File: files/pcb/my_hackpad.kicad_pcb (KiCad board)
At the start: 2 copper layers, 132 x 101.5 mm, 32 parts, among them SW1 CherryMX, SW10 CherryMX, SW11 CherryMX, SW12 CherryMX, SW13 CherryMX, SW14 CherryMX, SW15 CherryMX, SW16 RotaryEncoder_Switch, SW2 CherryMX, SW3 CherryMX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

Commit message: Actual gnd plane fixed
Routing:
- net GND: track 56.5 -> 0.00 mm
- added copper zone on B.Cu, net GND
- added copper zone on F.Cu, net GND
- removed copper zone on B.Cu, net (none)
- removed copper zone on F.Cu, net (none)
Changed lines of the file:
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@@
-	)
-	(segment
-		(start 131.306 59.17)
-		(end 133.806 61.67)
-		(width 0.25)
-		(layer "B.Cu")
-		(net 24)
-	)
-	(segment
-		(start 93.676015 50.66575)
-		(end 93.676015 57.100015)
-		(width 0.25)
-		(layer "B.Cu")
-		(net 24)
-	)
-	(segment
-		(start 98.032 59.182)
-		(end 98.044 59.17)
-		(width 0.25)
-		(layer "B.Cu")
-		(net 24)
-	)
-	(segment
-		(start 127.12 59.17)
-		(end 98.044 59.17)
-		(width 0.25)
-		(layer "B.Cu")
-		(net 24)
-	)
-	(segment
-		(start 95.758 59.182)
-		(end 98.032 59.182)
-		(width 0.25)
-		(layer "B.Cu")
-		(net 24)
-	)
-	(segment
-		(start 127.12 59.17)
-		(end 131.306 59.17)
-		(width 0.25)
-		(layer "B.Cu")
-		(net 24)
-	)
-	(segment
-		(start 133.806 61.67)
-		(end 141.62 61.67)
-		(width 0.25)
-		(layer "B.Cu")
-		(net 24)
-	)
-	(segment
-		(start 98.044 59.17)
-		(end 97.778 59.17)
-		(width 0.25)
-		(layer "B.Cu")
-		(net 24)
-	)
-	(segment
-		(start 93.676015 57.100015)
-		(end 95.758 59.182)
-		(width 0.25)
-		(layer "B.Cu")
-		(net 24)
 	)
 	(segment
@@
 	)
 	(zone
-		(net 0)
-		(net_name "")
+		(net 24)
+		(net_name "GND")
 		(layers "F&B.Cu")
 		(name "GND Plane")

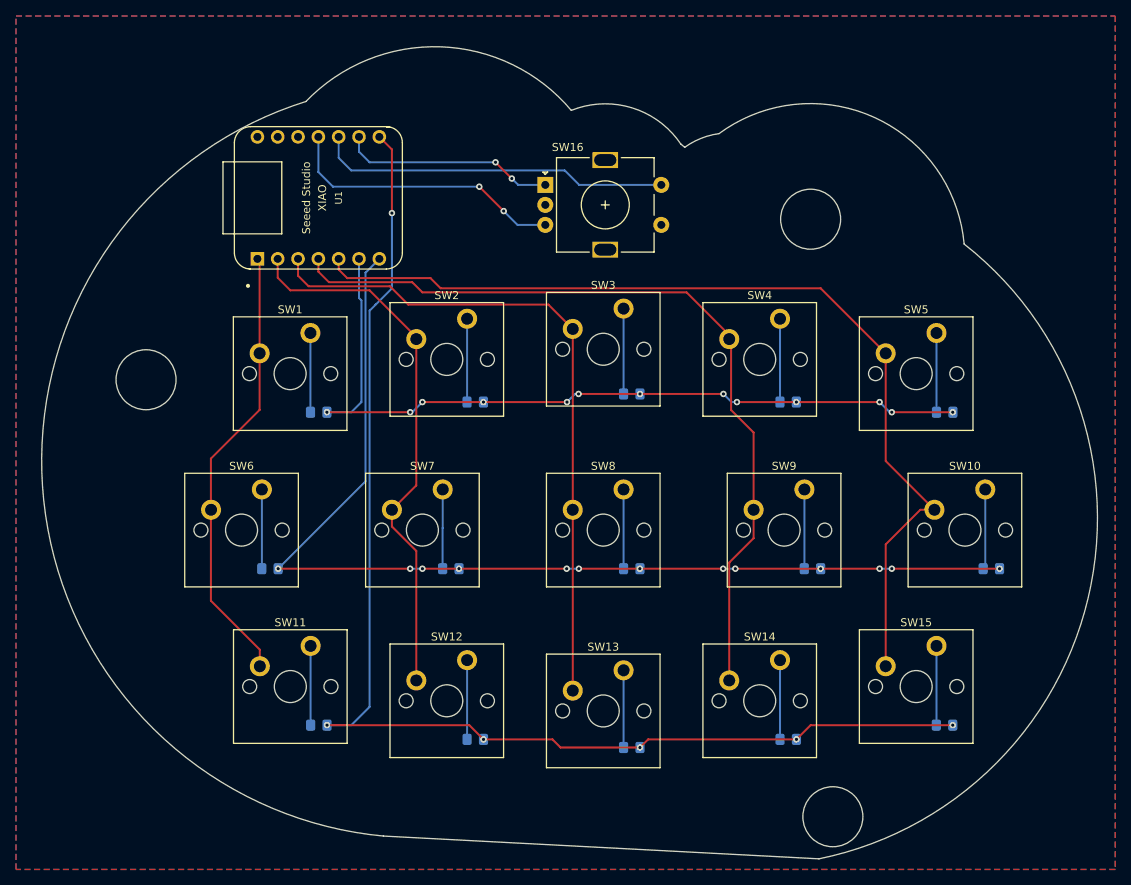
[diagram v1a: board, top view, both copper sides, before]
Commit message: PCB wire traces updated
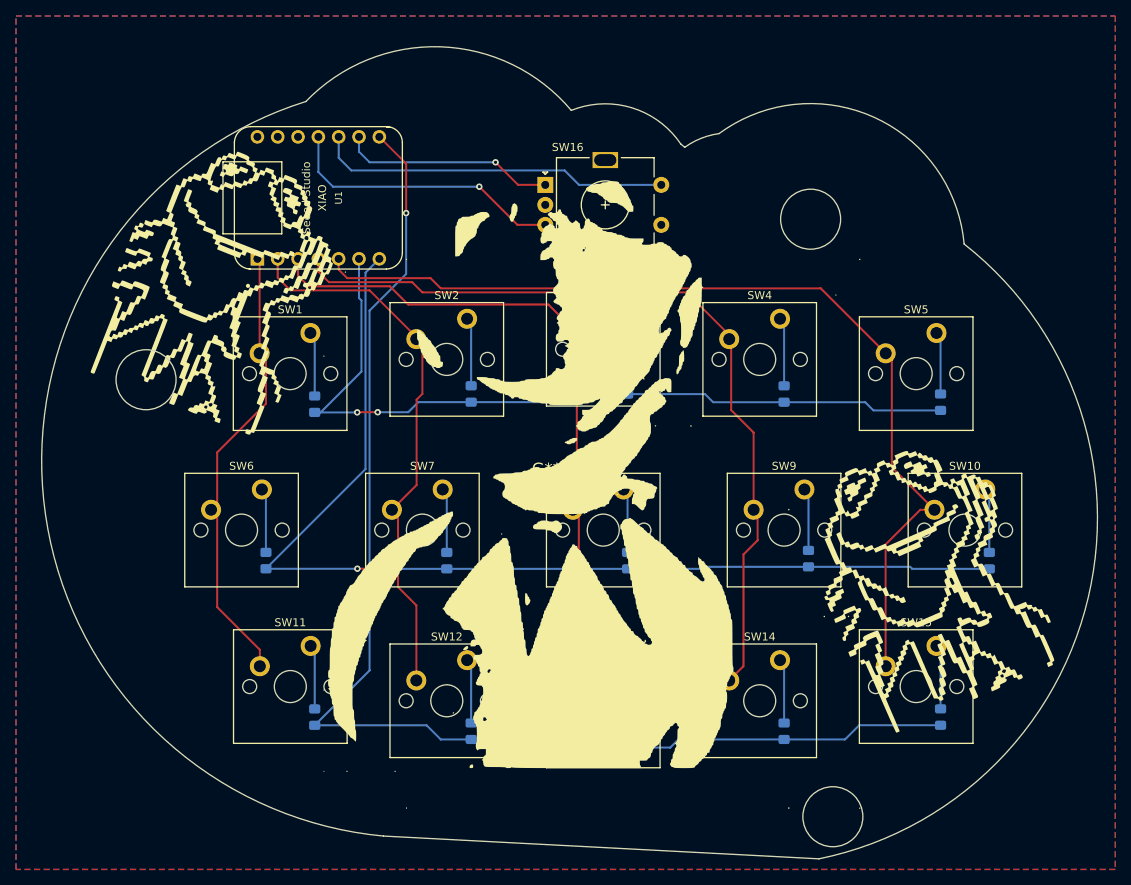
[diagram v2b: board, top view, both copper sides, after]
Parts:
- added G***: LOGO, LOGO, F.Cu at (127.8, 92.2)
- added G***: LOGO, LOGO, B.Cu at (123.5, 91.4)
- moved D5 1.36 mm to (176.5, 83.8), turned to 90 degrees
- moved D9 1.36 mm to (160.0, 103.4), turned to 90 degrees
- moved D13 1.14 mm to (137.4, 126.0), turned to 90 degrees
- moved D12 1.14 mm to (117.9, 125.0), turned to 90 degrees
- moved D14 1.14 mm to (157.0, 125.0), turned to 90 degrees
- moved D2 1.14 mm to (117.9, 82.8), turned to 90 degrees
- moved D6 1.13 mm to (92.2, 103.6), turned to 90 degrees
- moved D3 1.13 mm to (137.4, 81.8), turned to 90 degrees
- moved D8 1.13 mm to (137.4, 103.6), turned to 90 degrees
- moved D11 1.13 mm to (98.3, 123.2), turned to 90 degrees
- moved D15 1.13 mm to (176.5, 123.2), turned to 90 degrees
- moved D7 1.13 mm to (114.8, 103.6), turned to 90 degrees
- moved D4 1.13 mm to (157.0, 82.8), turned to 90 degrees
- moved D1 1.12 mm to (98.3, 84.1), turned to 90 degrees
- moved D10 1.04 mm to (182.6, 103.6), turned to 90 degrees
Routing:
- net Net-(D9-A): track 9.91 -> 7.83 mm
- net Net-(D5-A): track 9.91 -> 7.83 mm
- net Net-(D10-A): track 10.0 -> 8.08 mm
- net ROW1: track 134.1 -> 136.0 mm, vias 13 -> 2
- net Net-(D15-A): track 9.91 -> 8.08 mm
- net Net-(D6-A): track 9.91 -> 8.08 mm
- net Net-(D2-A): track 10.4 -> 8.58 mm
- net Net-(D13-A): track 9.65 -> 7.82 mm
- net Net-(D12-A): track 9.91 -> 8.08 mm
- net Net-(D14-A): track 9.91 -> 8.08 mm
- net Net-(D7-A): track 9.91 -> 8.08 mm
- net Net-(D4-A): track 10.4 -> 8.59 mm
- net Net-(D3-A): track 10.7 -> 8.85 mm
- net Net-(D8-A): track 9.91 -> 8.08 mm
- net Net-(D11-A): track 9.91 -> 8.08 mm
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
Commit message: Through holes fixed
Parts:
- added ?: , , F.Cu at (160.3, 61.0)
- added ?: , , F.Cu at (77.2, 81.0)
- added ?: , , F.Cu at (163.1, 135.7)
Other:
- outline, holes or cut-outs redrawn
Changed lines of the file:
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@@
 			(plotinvisibletext no)
 			(sketchpadsonfab no)
-			(subtractmaskfromsilk no)
+			(subtractmaskfromsilk yes)
 			(outputformat 1)
 			(mirror no)
-			(drillshape 1)
+			(drillshape 0)
 			(scaleselection 1)
 			(outputdirectory "")
@@
 	(net 28 "VCC")
 	(net 29 "3V3")
+	(footprint ""
+		(layer "F.Cu")
+		(at 160.288155 60.96)
+		(property "Reference" ""
+			(at 0 0 0)
+			(layer "F.SilkS")
+			(effects
+				(font
+					(size 1.27 1.27)
+					(thickness 0.15)
+				)
+			)
+		)
+		(property "Value" ""
+			(at 0 0 0)
+			(layer "F.Fab")
+			(effects
+				(font
+					(size 1.27 1.27)
+					(thickness 0.15)
+				)
+			)
+		)
+		(property "Footprint" ""
+			(at 0 0 0)
+			(layer "F.Fab")
+			(hide yes)
+			(effects
+				(font
+					(size 1.27 1.27)
+					(thickness 0.15)
+				)
+			)
+		)
+		(property "Datasheet" ""
+			(at 0 0 0)
+			(layer "F.Fab")
+			(hide yes)
+			(effects
+				(font
+					(size 1.27 1.27)
+					(thickness 0.15)
+				)
+			)
+		)
+		(property "Description" ""
+			(at 0 0 0)
+			(layer "F.Fab")
+			(hide yes)
+			(effects
+				(font
+					(size 1.27 1.27)
+					(thickness 0.15)
+				)
+			)
+		)
+		(pad "" np_thru_hole circle
+			(at 0 0)
+			(size 7.5 7.5)
+			(drill 7.5)
+			(layers "F&B.Cu" "*.Mask")
+		)
+	)
 	(footprint "Switch_Keyboard_Cherry_MX:SW_Cherry_MX_PCB_1.00u"
 		(layer "F.Cu")
@@
 		)
 	)
+	(footprint ""
+		(layer "F.Cu")
+		(at 77.216 81.026)
+		(property "Reference" ""
+			(at 0 0 0)
+			(layer "F.SilkS")
+			(effects
+				(font
+					(size 1.27 1.27)
+					(thickness 0.15)
+				)
+			)
+		)
+		(property "Value" ""
+			(at 0 0 0)
+			(layer "F.Fab")
+			(effects
+				(font
+					(size 1.27 1.27)
+					(thickness 0.15)
+				)
+			)
+		)
+		(property "Footprint" ""
+			(at 0 0 0)
+			(layer "F.Fab")
+			(hide yes)
+			(effects
+				(font
+					(size 1.27 1.27)
+					(thickness 0.15)
+				)
+			)
+		)
+		(property "Datasheet" ""
+			(at 0 0 0)
+			(layer "F.Fab")
+			(hide yes)
+			(effects
+				(font
+					(size 1.27 1.27)
+					(thickness 0.15)
+				)
+			)
+		)
+		(property "Description" ""
+			(at 0 0 0)
+			(layer "F.Fab")
+			(hide yes)
+			(effects
+				(font
+					(size 1.27 1.27)
+					(thickness 0.15)
+				)
+			)
+		)
+		(pad "" np_thru_hole circle
+			(at 0 0)
+			(size 7.5 7.5)
+			(drill 7.5)
+			(layers "F&B.Cu" "*.Mask")
+		)
+	)
 	(footprint "Seeed Studio XIAO Series Library:XIAO-Generic-Thruhole-14P-2.54-21X17.8MM"
 		(layer "F.Cu")
@@
 		)
 	)
+	(footprint ""
+		(layer "F.Cu")
+		(at 163.068 135.650155)
+		(property "Reference" ""
+			(at 0 0 0)
+			(layer "F.SilkS")
+			(effects
+				(font
+					(size 1.27 1.27)
+					(thickness 0.15)
+				)
+			)
+		)
+		(property "Value" ""
+			(at 0 0 0)
+			(layer "F.Fab")
+			(effects
+				(font
+					(size 1.27 1.27)
+					(thickness 0.15)
+				)
+			)
+		)
+		(property "Footprint" ""
+			(at 0 0 0)
+			(layer "F.Fab")
+			(hide yes)
+			(effects
+				(font
+					(size 1.27 1.27)
+					(thickness 0.15)
+				)
+			)
+		)
+		(property "Datasheet" ""
+			(at 0 0 0)
+			(layer "F.Fab")
+			(hide yes)
+			(effects
+				(font
+					(size 1.27 1.27)
+					(thickness 0.15)
+				)
+			)
+		)
+		(property "Description" ""
+			(at 0 0 0)
+			(layer "F.Fab")
+			(hide yes)
+			(effects
+				(font
+					(size 1.27 1.27)
+					(thickness 0.15)
+				)
+			)
+		)
+		(pad "" np_thru_hole circle
+			(at 0 0)
+			(size 7.5 7.5)
+			(drill 7.5)
+			(layers "F&B.Cu" "*.Mask")
+		)
+	)
 	(footprint "Switch_Keyboard_Cherry_MX:SW_Cherry_MX_PCB_1.00u"
 		(layer "F.Cu")
@@
 		)
 	)
-	(gr_circle
-		(center 163.068 135.650155)
-		(end 166.818 135.650155)
-		(stroke
-			(width 0.1)
-			(type default)
-		)
-		(fill none)
-		(layer "Edge.Cuts")
-	)
-	(gr_circle
-		(center 77.216 81.026)
-		(end 80.966 81.026)
-		(stroke
-			(width 0.1)
-			(type default)
-		)
-		(fill none)
-		(layer "Edge.Cuts")
-	)
 	(gr_arc
 		(start 179.477871 64.064274)
@@
 		(layer "Edge.Cuts")
 	)
-	(gr_circle
-		(center 160.288155 60.96)
-		(end 164.038155 60.96)
-		(stroke
-			(width 0.1)
-			(type default)
-		)
-		(fill none)
-		(layer "Edge.Cuts")
-	)
